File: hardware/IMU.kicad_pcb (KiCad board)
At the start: 2 copper layers, 37 parts, among them J1 Conn_01x10, J3 USB_B_Micro, J4 Conn_01x10, J6 UART, J8 IMU_Headers, J9 SWD, SW1 SW_Push, U2 HT75xx-1-SOT89, U3 ISM330DLCTR, U4 STM32F401RCT6TR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

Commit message: layout
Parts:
- moved C12 0.50 mm to (118.5, 80.0)
- moved J8 0.50 mm to (116.3, 75.5)
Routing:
- net GND: track 0.00 -> 79.6 mm, vias 0 -> 7
- net +3V3: track 21.2 -> 52.8 mm, vias 0 -> 15
- net /SDA: track 17.3 -> 19.0 mm
- net /SCL: track 21.2 -> 22.7 mm
- added copper zone on B.Cu, net +3V3
- added copper zone on F.Cu, net GND

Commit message: layout completed
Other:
- board outline added: 85 x 75 mm
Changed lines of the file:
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@@
 		)
+	)
+	(gr_rect
+		(start 70 55)
+		(end 155 130)
+		(stroke
+			(width 0.05)
+			(type default)
+		)
+		(fill no)
+		(layer "Edge.Cuts")
 	)
 	(segment
@@
 		(hatch edge 0.5)
 		(connect_pads
-			(clearance 0.5)
+			(clearance 0.2)
 		)
-		(min_thickness 0.25)
+		(min_thickness 0.2)
 		(filled_areas_thickness no)
 		(fill
-			(thermal_gap 0.5)
+			(thermal_gap 0.2)
 			(thermal_bridge_width 0.5)
 		)
@@
 		(priority 1)
 		(connect_pads
-			(clearance 0.5)
+			(clearance 0.2)
 		)
-		(min_thickness 0.25)
+		(min_thickness 0.2)
 		(filled_areas_thickness no)
 		(fill
-			(thermal_gap 0.5)
+			(thermal_gap 0.2)
 			(thermal_bridge_width 0.5)
 		)

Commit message: fixed errors
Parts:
- moved C3 38.0 mm to (122.8, 84.2)
- moved C2 37.3 mm to (109.4, 99.8)
- moved C4 34.6 mm to (115.4, 98.1)
- moved C5 23.2 mm to (105.1, 94.9)
- moved C6 14.3 mm to (111.1, 80.4)
- moved J3 12.2 mm to (88.9, 117.8)
- moved C7 10.5 mm to (105.6, 84.3)
- moved J6 6.44 mm to (95.3, 103.0)
- moved C11 5.55 mm to (110.8, 74.5)
- moved C12 5.55 mm to (118.3, 74.5)
- moved U3 5.55 mm to (114.8, 74.5)
- moved J8 5.40 mm to (116.1, 70.1)
- moved C8 3.84 mm to (121.5, 99.8)
- moved C9 2.92 mm to (101.7, 94.1)
- moved C10 2.46 mm to (102.5, 98.5)
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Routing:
- net GND: track 79.6 -> 63.4 mm
- net +5V: track 3.97 -> 17.1 mm
- net /TX: track 9.95 -> 16.2 mm
- net /INT1: track 17.1 -> 23.2 mm
- net /SCL: track 22.7 -> 28.4 mm
- net /SDA: track 19.0 -> 24.6 mm
- net /INT2: track 16.9 -> 22.4 mm
- net /RX: track 7.77 -> 12.9 mm
- net +3V3: track 52.8 -> 57.4 mm, vias 15 -> 16
- net Net-(U4-VCAP_1): track 4.86 -> 6.31 mm
- net /RST: track 39.6 -> 40.3 mm

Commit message: added spi
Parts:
- removed U3: ISM330DLCTR, My_library:PQFN50P250X300X86-14N
- added J2: Conn_01x06, Connector_PinHeader_2.54mm:PinHeader_1x06_P2.54mm_Vertical, F.Cu at (122.5, 117.0)
- J4: value Conn_01x10 -> SPI_Headers; footprint Connector_PinHeader_2.54mm:PinHeader_1x10_P2.54mm_Vertical -> Connector_PinHeader_2.54mm:PinHeader_1x04_P2.54mm_Vertical
- moved J4 7.62 mm to (117.5, 117.0), turned to -90 degrees
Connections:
- C11 pad 1: +3V3 -> /PWR
- C12 pad 1: +3V3 -> /PWR
- C2 pad 1: +3V3 -> /PWR
- C3 pad 1: +3V3 -> /PWR
- C4 pad 1: +3V3 -> /PWR
- C5 pad 1: +3V3 -> /PWR
- C6 pad 1: +3V3 -> /PWR
- C7 pad 1: +3V3 -> /PWR
- D2 pad 2: +3V3 -> /PWR
- J4 pad 1: /PA4 -> /SPI1_MOSI
- J4 pad 2: /PA5 -> /SPI1_MISO
- J4 pad 3: /PA6 -> /SPI_SCK
- J4 pad 4: /PA7 -> /SPI1_CS
- J6 pad 1: +3V3 -> /PWR
- J8 pad 3: +3V3 -> /PWR
- J9 pad 1: +3V3 -> /PWR
- R1 pad 1: +3V3 -> /PWR
- U4 pad 1: +3V3 -> /PWR
- U4 pad 19: +3V3 -> /PWR
- U4 pad 20: /PA4 -> /SPI1_CS
- U4 pad 21: /PA5 -> /SPI_SCK
- U4 pad 22: /PA6 -> /SPI1_MISO
- U4 pad 23: /PA7 -> /SPI1_MOSI
- U4 pad 32: +3V3 -> /PWR
- U4 pad 33: Net-(J4-Pin_7) -> Net-(J2-Pin_2)
- U4 pad 34: Net-(J4-Pin_8) -> Net-(J2-Pin_3)
- U4 pad 35: Net-(J4-Pin_9) -> Net-(J2-Pin_4)
- U4 pad 36: Net-(J4-Pin_10) -> Net-(J2-Pin_5)
- U4 pad 48: +3V3 -> /PWR
- U4 pad 64: +3V3 -> /PWR
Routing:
- net /PWR: track 0.00 -> 41.1 mm, vias 0 -> 15
- net +3V3: track 57.4 -> 18.7 mm, vias 16 -> 2
- net Net-(J4-Pin_10): track 30.8 -> 0.00 mm
- net Net-(J2-Pin_5): track 0.00 -> 30.8 mm
- net Net-(J4-Pin_9): track 29.2 -> 0.00 mm
- net Net-(J2-Pin_4): track 0.00 -> 29.2 mm
- net Net-(J4-Pin_8): track 27.6 -> 0.00 mm
- net Net-(J2-Pin_3): track 0.00 -> 27.6 mm
- net Net-(J4-Pin_7): track 26.0 -> 0.00 mm
- net Net-(J2-Pin_2): track 0.00 -> 26.0 mm
- net /SPI1_MOSI: track 0.00 -> 23.1 mm
- net /PA7: track 23.1 -> 0.00 mm
- net /SPI1_MISO: track 0.00 -> 22.2 mm
- net /PA6: track 22.2 -> 0.00 mm
- net /SPI1_CS: track 0.00 -> 22.1 mm
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
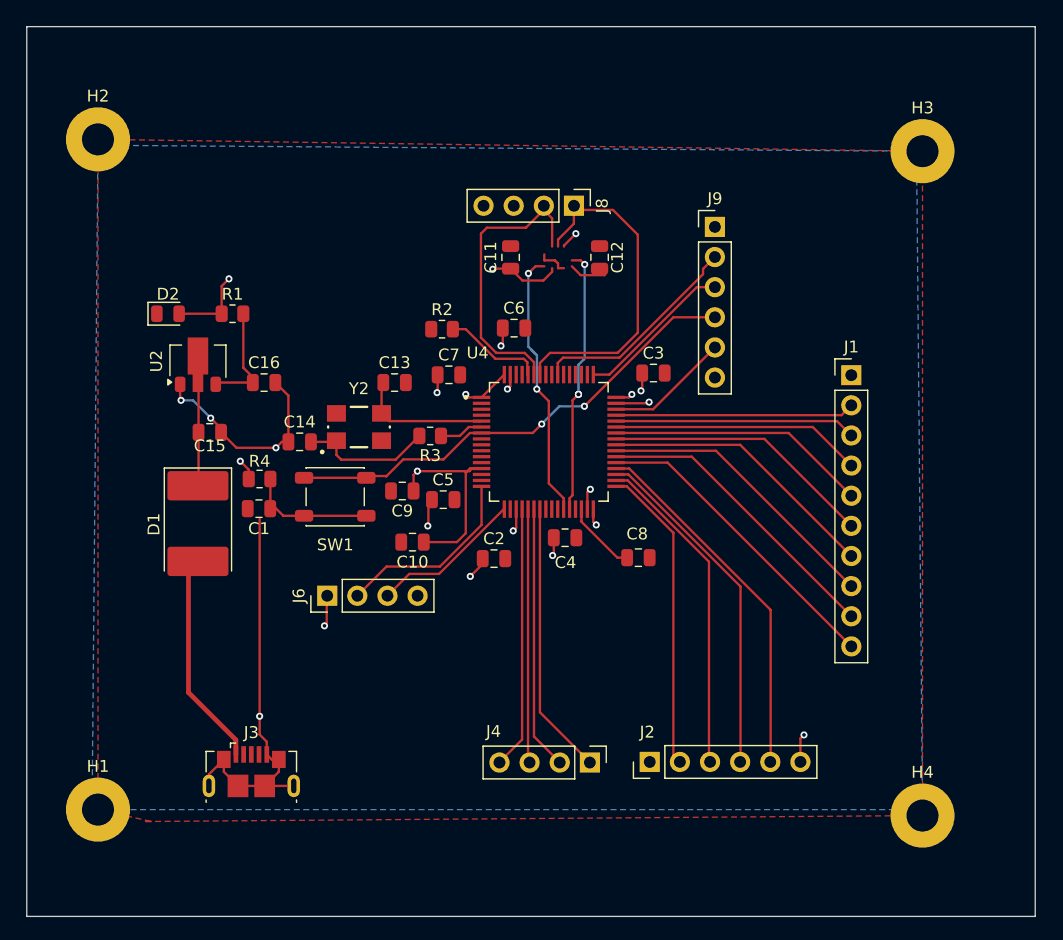
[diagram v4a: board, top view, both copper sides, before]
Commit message: Fixed IMU
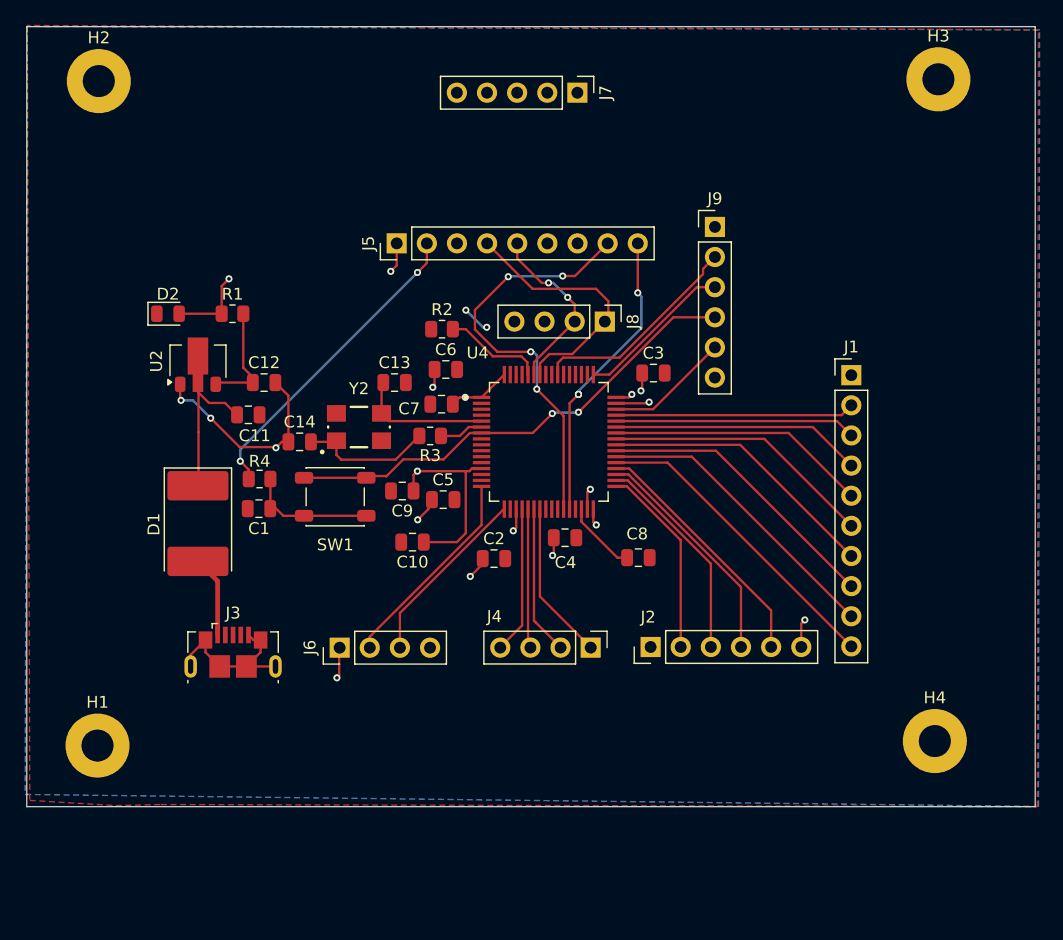
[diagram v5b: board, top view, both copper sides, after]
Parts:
- removed the C11 at (110.8, 74.5)
- removed the C12 at (118.3, 74.5)
- added J5: Conn_01x09, Connector_PinHeader_2.54mm:PinHeader_1x09_P2.54mm_Vertical, F.Cu at (101.2, 73.3)
- added J7: Conn_01x05, Connector_PinHeader_2.54mm:PinHeader_1x05_P2.54mm_Vertical, F.Cu at (116.4, 60.6)
- moved J3 10.2 mm to (87.4, 107.7)
- moved J8 10.1 mm to (118.7, 79.9)
- moved J2 9.69 mm to (122.6, 107.3)
- moved J4 9.69 mm to (117.5, 107.3)
- moved C6 6.73 mm to (105.3, 83.9)
- moved H4 6.37 mm to (146.5, 115.2)
- moved H3 6.21 mm to (146.8, 59.4)
- moved H1 5.40 mm to (76.0, 115.6)
- moved H2 4.91 mm to (76.1, 59.6)
- moved J6 4.50 mm to (96.4, 107.3)
- moved C11 3.57 mm to (88.7, 87.7)
- moved C7 2.55 mm to (105.0, 86.8), turned to 180 degrees
- renumbered C15 to C11, C16 to C12
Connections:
- C10 pad 1: +3V3 -> /PWR
- C9 pad 1: +3V3 -> /PWR
- U4 pad 13: +3V3 -> /PWR
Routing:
- net GND: track 60.7 -> 38.8 mm
- net /INT1: track 23.2 -> 35.2 mm, vias 2 -> 4
- net +5V: track 17.1 -> 6.89 mm
- net /SPI1_CS: track 22.1 -> 12.4 mm
- net Net-(J2-Pin_4): track 29.2 -> 19.5 mm
- net Net-(J2-Pin_5): track 30.8 -> 21.1 mm
- net /SPI1_MISO: track 22.2 -> 12.6 mm
- net /SPI1_MOSI: track 23.1 -> 13.4 mm
- net /SDA: track 24.6 -> 15.1 mm, vias 0 -> 2
- net Net-(J2-Pin_3): track 27.6 -> 18.1 mm
- net /SPI_SCK: track 21.4 -> 11.9 mm
- net Net-(J2-Pin_2): track 26.0 -> 17.2 mm
- net +3V3: track 18.7 -> 26.7 mm
- net /PWR: track 41.1 -> 48.9 mm, vias 15 -> 14
- net /SCL: track 28.4 -> 22.0 mm
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- added copper zone on B.Cu, net /PWR
- removed copper zone on B.Cu, net +3V3
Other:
- board size 85 x 75 mm -> 85 x 65.8 mm

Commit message: finished layout
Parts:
- moved H1 6.68 mm to (75.9, 108.9)
- moved H4 6.30 mm to (146.8, 108.9)
- moved H3 1.89 mm to (147.1, 61.3)
- moved H2 1.72 mm to (76.2, 61.3)
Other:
- board size 85 x 65.8 mm -> 85 x 59.5 mm
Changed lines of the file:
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@@
 	(footprint "MountingHole:MountingHole_2.7mm_M2.5_Pad"
 		(layer "F.Cu")
-		(at 146.84 59.44)
+		(at 147.08 61.31)
 		(descr "Mounting Hole 2.7mm, M2.5, generated by kicad-footprint-generator mountinghole.py")
 		(tags "mountinghole M2.5")
@@
 	(footprint "MountingHole:MountingHole_2.7mm_M2.5_Pad"
 		(layer "F.Cu")
-		(at 146.54 115.22)
+		(at 146.78 108.92)
 		(descr "Mounting Hole 2.7mm, M2.5, generated by kicad-footprint-generator mountinghole.py")
 		(tags "mountinghole M2.5")
@@
 	(footprint "MountingHole:MountingHole_2.7mm_M2.5_Pad"
 		(layer "F.Cu")
-		(at 75.96 115.6)
+		(at 75.9 108.92)
 		(descr "Mounting Hole 2.7mm, M2.5, generated by kicad-footprint-generator mountinghole.py")
 		(tags "mountinghole M2.5")
@@
 	(footprint "MountingHole:MountingHole_2.7mm_M2.5_Pad"
 		(layer "F.Cu")
-		(at 76.07 59.59)
+		(at 76.2 61.31)
 		(descr "Mounting Hole 2.7mm, M2.5, generated by kicad-footprint-generator mountinghole.py")
 		(tags "mountinghole M2.5")
@@
 		(tags "Through hole pin header THT 1x04 2.54mm single row")
 		(property "Reference" "J8"
-			(at 0 -2.38 90)
+			(at -2.29 -1.28 180)
 			(layer "F.SilkS")
 			(effects
@@
 	(gr_rect
 		(start 70 55)
-		(end 155 120.75)
+		(end 155 114.52)
 		(stroke
 			(width 0.05)
@@
 		(polygon
 			(pts
-				(xy 81.3 120.57) (xy 155.18 120.75) (xy 155.27 55.27) (xy 70.04 54.9) (xy 70.25 120.22) (xy 77.5 120.66)
+				(xy 82.1 114.47) (xy 154.61 114.6) (xy 155.27 55.27) (xy 70.04 54.9) (xy 69.83 114.52) (xy 78.3 114.56)
 			)
 		)
@@
 		(polygon
 			(pts
-				(xy 69.86 119.72) (xy 155.27 120.73) (xy 155.37 55.27) (xy 70.05 54.99)
+				(xy 69.74 113.94) (xy 155.15 114.95) (xy 155.37 55.27) (xy 70.05 54.99)
 			)
 		)
